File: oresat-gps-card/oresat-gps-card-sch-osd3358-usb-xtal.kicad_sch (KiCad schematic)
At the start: 42 parts, among them U1 OSD3358-512M-BSM, U11 RCLAMP0504FB, Y1 24MHz, Y2 Crystal

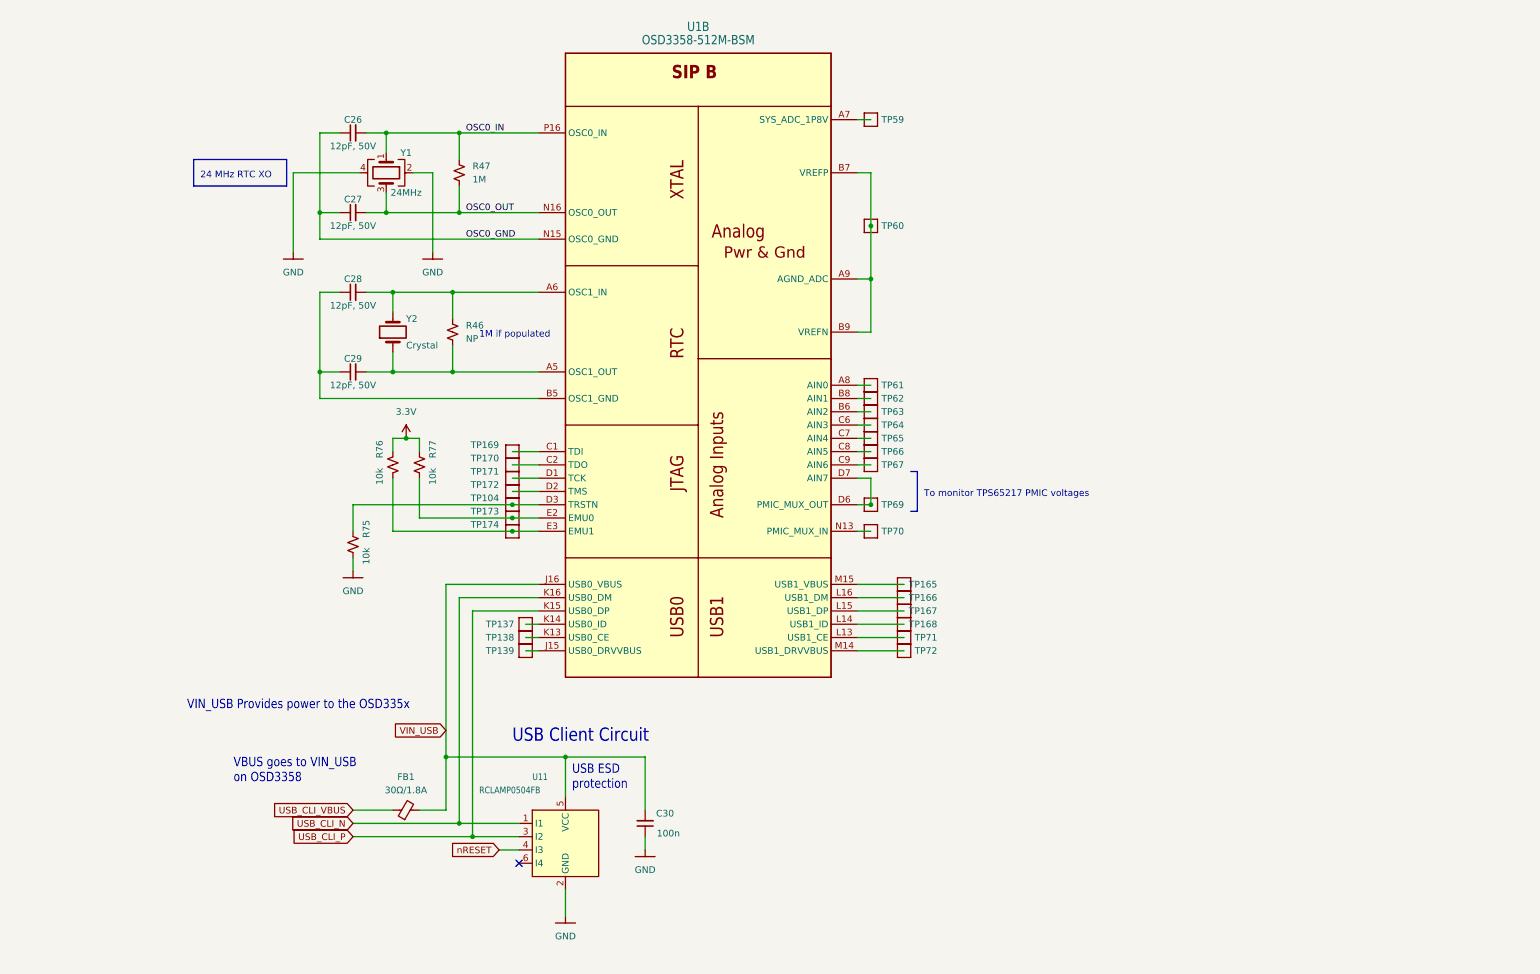
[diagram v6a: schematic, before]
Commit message: updated symbols and started new 2771 symbol
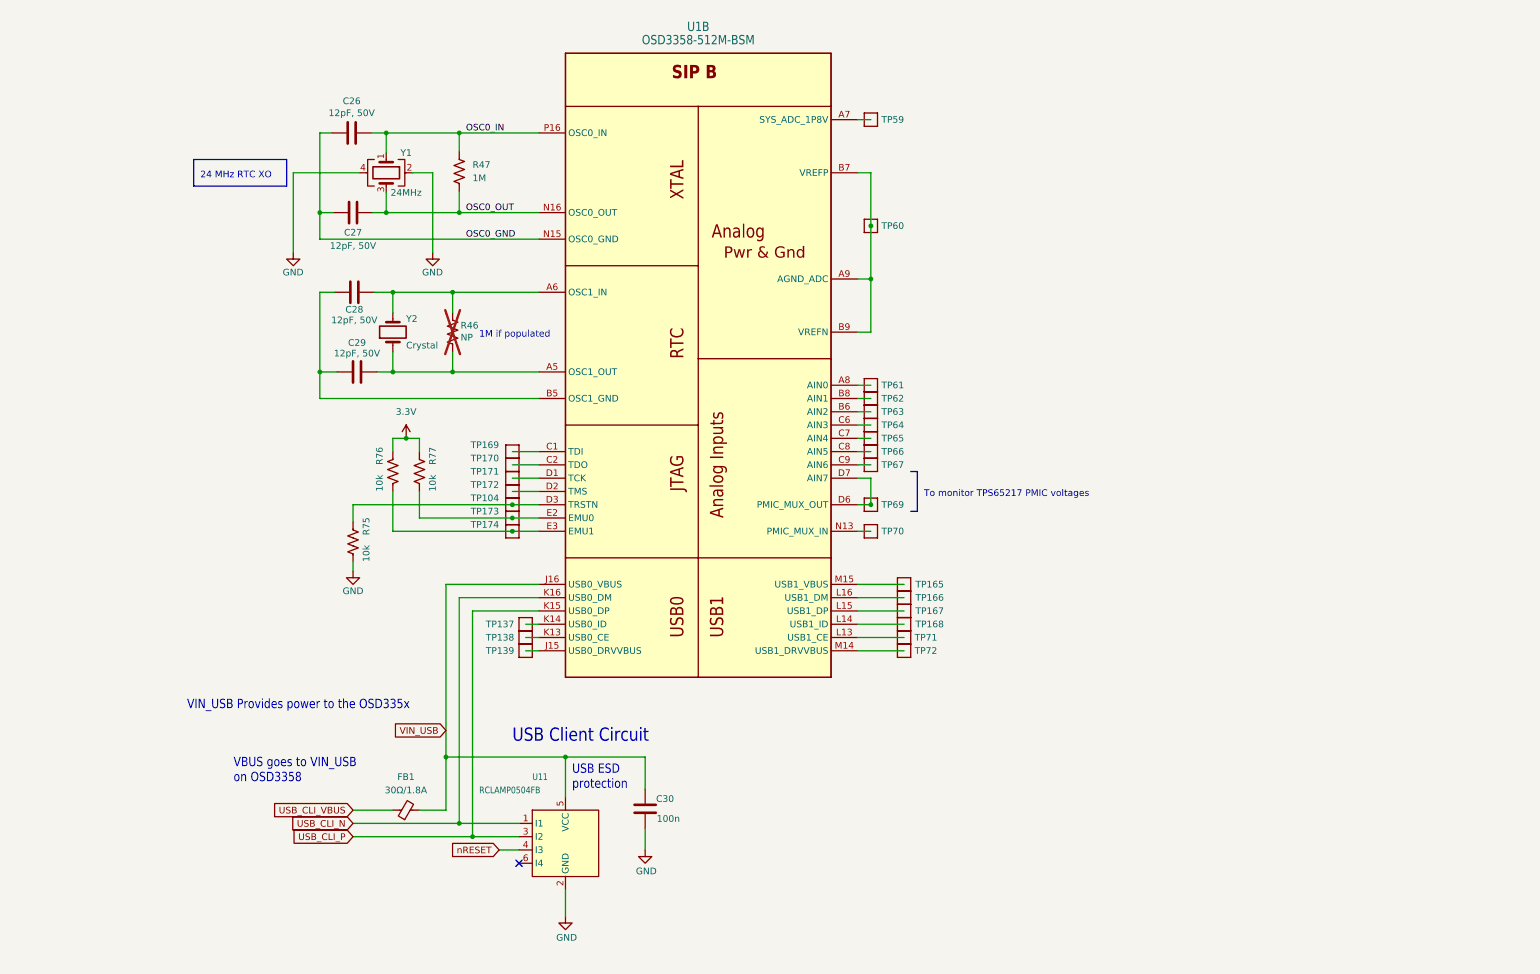
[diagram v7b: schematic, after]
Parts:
- C26, C27, C28, C29, C30: symbol Device:C_Small -> Device:C
- R46: symbol Device:R_Small_US -> Device:R_US; now not fitted
- R47, R75, R76, R77: symbol Device:R_Small_US -> Device:R_US
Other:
- moved on the sheet: C29, C30
